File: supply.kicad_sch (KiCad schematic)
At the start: 10 parts, among them U2 AP62301WU-7

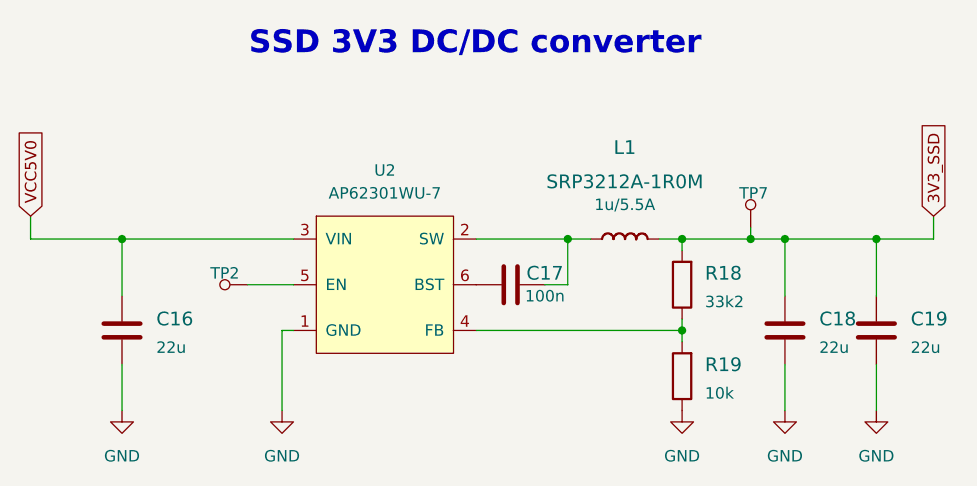
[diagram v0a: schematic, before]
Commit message: Update AP62301WU-7 symbol and footprint
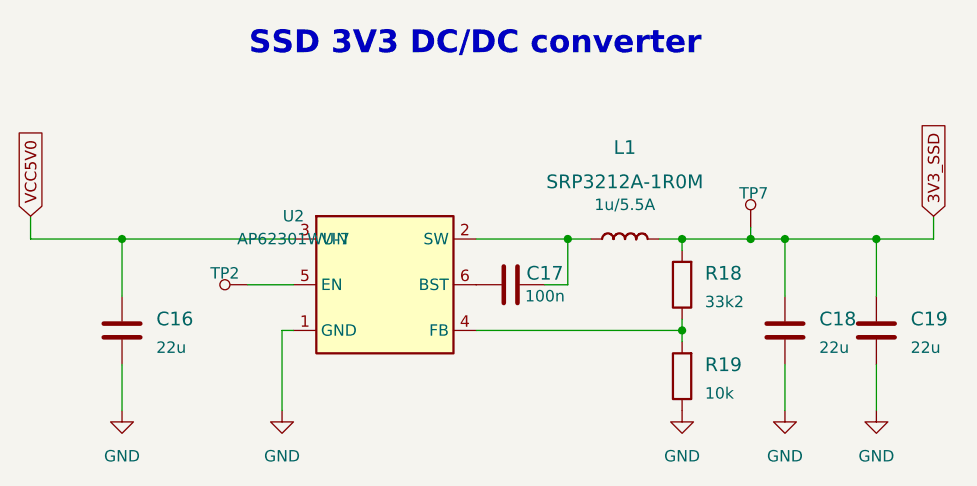
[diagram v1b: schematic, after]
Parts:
- U2: footprint scalenode-cm4-baseboard-footprints:TSOT23-6 -> antmicro-footprints:AP62301WU-7-TSOT23-6; symbol scalenode-cm4-baseboard:AP62301WU-7 -> antmicroDCDCConverters:AP62301WU-7; Author (none) -> Antmicro; Copyright (none) -> Copyright (c) 2023 Antmicro; License (none) -> Apache-2.0
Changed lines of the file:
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@@
     (pin "1")
   )
-  (symbol (lib_id "scalenode-cm4-baseboard:AP62301WU-7") (at 195.58 147.32 0) (unit 1)
+  (symbol (lib_id "antmicroDCDCConverters:AP62301WU-7") (at 185.42 152.4 0) (unit 1)
     (in_bom yes) (on_board yes) (fields_autoplaced)
-    (property "Reference" "U2" (id 0) (at 195.58 134.62 0))
-    (property "Value" "AP62301WU-7" (id 1) (at 195.58 137.16 0))
-    (property "Footprint" "scalenode-cm4-baseboard-footprints:TSOT23-6" (id 2) (at 194.31 163.83 0)
+    (property "Reference" "U2" (id 0) (at 185.42 139.7 0))
+    (property "Value" "AP62301WU-7" (id 1) (at 185.42 142.24 0))
+    (property "Footprint" "antmicro-footprints:AP62301WU-7-TSOT23-6" (id 2) (at 220.98 149.86 0)
+      (effects (font (size 1.27 1.27) (thickness 0.15)) (justify left bottom) hide)
+    )
+    (property "Datasheet" "https://www.diodes.com/assets/Datasheets/AP62300_AP62301_AP62300T.pdf" (id 3) (at 220.98 152.4 0)
+      (effects (font (size 1.27 1.27) (thickness 0.15)) (justify left bottom) hide)
+    )
+    (property "MPN" "AP62301WU-7" (id 4) (at 220.98 154.94 0)
+      (effects (font (size 1.27 1.27) (thickness 0.15)) (justify left bottom) hide)
+    )
+    (property "Manufacturer" "Diodes Incorporated" (id 5) (at 220.98 157.48 0)
+      (effects (font (size 1.27 1.27) (thickness 0.15)) (justify left bottom) hide)
+    )
+    (property "Author" "Antmicro" (id 6) (at 220.98 160.02 0)
+      (effects (font (size 1.27 1.27) (thickness 0.15)) (justify left bottom) hide)
+    )
+    (property "License" "Apache-2.0" (id 7) (at 220.98 162.56 0)
+      (effects (font (size 1.27 1.27) (thickness 0.15)) (justify left bottom) hide)
+    )
+    (property "Copyright" "Copyright (c) 2023 Antmicro" (id 8) (at 185.42 152.4 0)
       (effects (font (size 1.27 1.27)) hide)
     )
-    (property "Datasheet" "https://www.diodes.com/assets/Datasheets/AP62300_AP62301_AP62300T.pdf" (id 3) (at 194.31 156.21 0)
-      (effects (font (size 1.27 1.27)) hide)
-    )
-    (property "MPN" "AP62301WU-7" (id 4) (at 194.31 161.29 0)
-      (effects (font (size 1.27 1.27)) hide)
-    )
-    (property "Manufacturer" "Diodes Incorporated" (id 5) (at 194.31 158.75 0)
-      (effects (font (size 1.27 1.27)) hide)
-    )

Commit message: Delete copyright field
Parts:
- U2: Copyright Copyright (c) 2023 Antmicro -> (none)
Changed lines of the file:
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@@
   )
   (symbol (lib_id "antmicroDCDCConverters:AP62301WU-7") (at 185.42 152.4 0) (unit 1)
-    (in_bom yes) (on_board yes) (fields_autoplaced)
-    (property "Reference" "U2" (id 0) (at 185.42 139.7 0))
-    (property "Value" "AP62301WU-7" (id 1) (at 185.42 142.24 0))
+    (in_bom yes) (on_board yes)
+    (property "Reference" "U2" (id 0) (at 195.072 134.366 0))
+    (property "Value" "AP62301WU-7" (id 1) (at 195.326 136.906 0))
     (property "Footprint" "antmicro-footprints:AP62301WU-7-TSOT23-6" (id 2) (at 220.98 149.86 0)
       (effects (font (size 1.27 1.27) (thickness 0.15)) (justify left bottom) hide)
@@
       (effects (font (size 1.27 1.27) (thickness 0.15)) (justify left bottom) hide)
     )
-    (property "Copyright" "Copyright (c) 2023 Antmicro" (id 8) (at 185.42 152.4 0)
-      (effects (font (size 1.27 1.27)) hide)
-    )
     (pin "1")

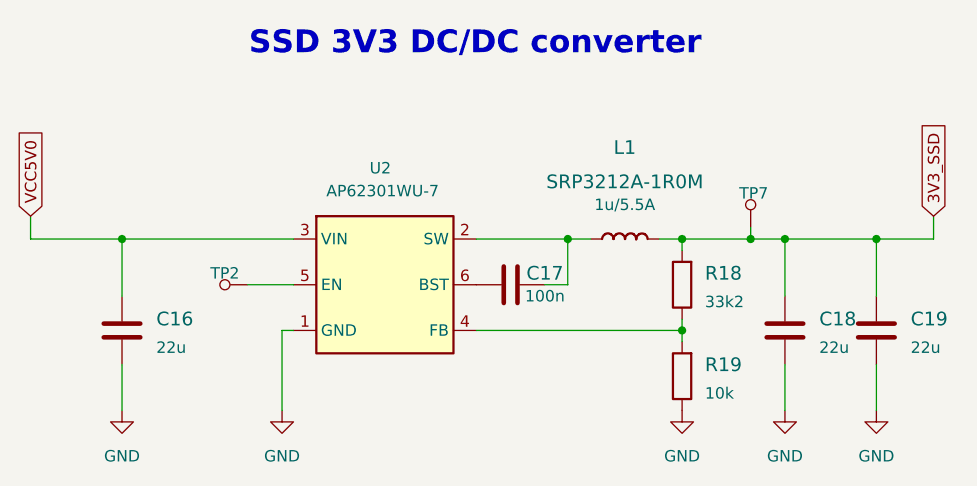
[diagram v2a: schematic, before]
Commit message: Update C1,C2,C3 symbol and footprint
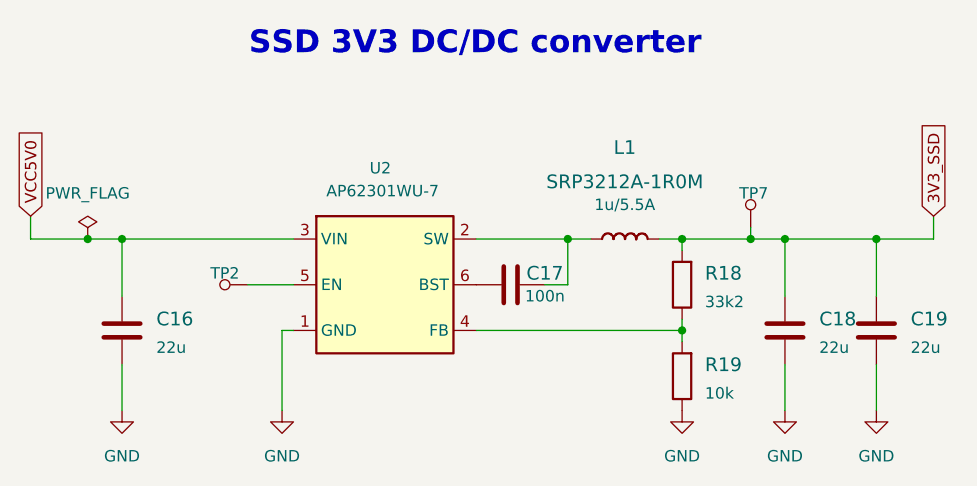
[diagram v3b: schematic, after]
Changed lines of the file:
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@@
   (junction (at 250.19 142.24) (diameter 0) (color 0 0 0 0)
   )
+  (junction (at 162.56 142.24) (diameter 0) (color 0 0 0 0)
+  )
   (junction (at 228.6 152.4) (diameter 0) (color 0 0 0 0)
   )
@@
     (stroke (width 0) (type default) (color 0 0 0 0))
   )
+  (wire (pts (xy 162.56 142.24) (xy 166.37 142.24))
+    (stroke (width 0) (type default) (color 0 0 0 0))
+  )
   (wire (pts (xy 156.21 139.7) (xy 156.21 142.24))
     (stroke (width 0) (type default) (color 0 0 0 0))
@@
     (stroke (width 0) (type default) (color 0 0 0 0))
   )
-  (wire (pts (xy 156.21 142.24) (xy 166.37 142.24))
+  (wire (pts (xy 156.21 142.24) (xy 162.56 142.24))
     (stroke (width 0) (type default) (color 0 0 0 0))
   )
@@
     )
     (pin "1")
+  )
+  (symbol (lib_id "antmicropower:PWR_FLAG") (at 162.56 142.24 0) (unit 1)
+    (in_bom yes) (on_board yes) (fields_autoplaced)
+    (property "Reference" "#FLG0101" (id 0) (at 162.56 140.335 0)
+      (effects (font (size 1.27 1.27)) hide)
+    )
+    (property "Value" "PWR_FLAG" (id 1) (at 162.56 137.16 0))
+    (property "Footprint" "" (id 2) (at 162.56 142.24 0)
+      (effects (font (size 1.27 1.27)) hide)
+    )
+    (property "Datasheet" "" (id 3) (at 162.56 142.24 0)
+      (effects (font (size 1.27 1.27)) hide)
+    )
+    (pin "1")

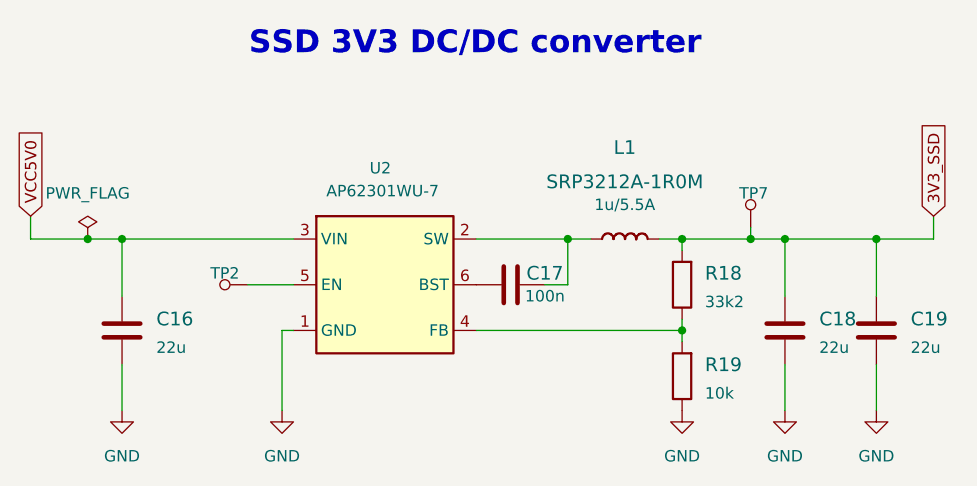
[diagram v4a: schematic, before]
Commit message: Update C13, C17, C21, C37, C51, C54, C55, C56 symbol and footprint
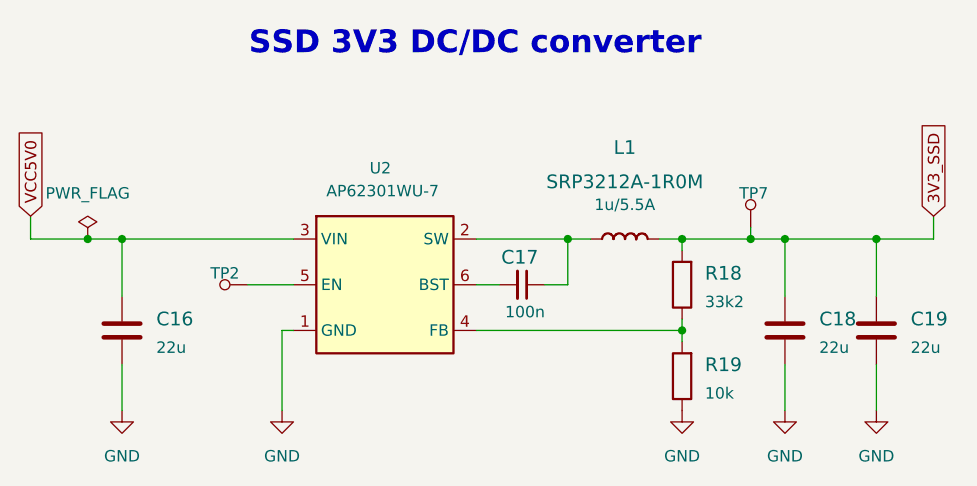
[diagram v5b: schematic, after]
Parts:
- C17: footprint scalenode-cm4-baseboard-footprints:0402-cap -> antmicro-footprints:C_0402_1005Metric; symbol scalenode-cm4-baseboard:C_100n_0402 -> antmicroCapacitors0402:C_100n_0402; Author (none) -> Antmicro; Dielectric (none) -> X5R; License (none) -> Apache-2.0; Voltage (none) -> 50V
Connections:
- net at L1.1 (P), U2.2 (SW): now also C17.1; no longer C17.2
- net at U2.6 (BST): now also C17.2; no longer C17.1
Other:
- moved on the sheet: C17
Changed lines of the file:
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@@
+    (stroke (width 0) (type default) (color 0 0 0 0))
+  )
+  (wire (pts (xy 205.74 147.32) (xy 208.28 147.32))
     (stroke (width 0) (type default) (color 0 0 0 0))
   )
@@
     (pin "1")
   )
-  (symbol (lib_id "scalenode-cm4-baseboard:C_100n_0402") (at 209.55 147.32 90) (unit 1)
+  (symbol (lib_id "antmicroCapacitors0402:C_100n_0402") (at 213.36 147.32 180) (unit 1)
     (in_bom yes) (on_board yes)
-    (property "Reference" "C17" (id 0) (at 213.36 146.05 90)
+    (property "Reference" "C17" (id 0) (at 210.566 144.272 0)
       (effects (font (size 1.524 1.524)))
     )
-    (property "Value" "C_100n_0402" (id 1) (at 213.36 147.32 0)
+    (property "Value" "C_100n_0402" (id 1) (at 213.36 143.51 0)
       (effects (font (size 1.524 1.524)) hide)
     )
-    (property "Footprint" "scalenode-cm4-baseboard-footprints:0402-cap" (id 2) (at 204.47 142.24 0)
-      (effects (font (size 1.524 1.524)) (justify left) hide)
-    )
-    (property "Datasheet" "" (id 3) (at 209.55 147.32 0)
-      (effects (font (size 1.27 1.27)) hide)
-    )
-    (property "Manufacturer" "Murata" (id 4) (at 199.39 142.24 0)
-      (effects (font (size 1.524 1.524)) (justify left) hide)
-    )
-    (property "MPN" "GRM155R61H104KE14D" (id 5) (at 201.93 142.24 0)
-      (effects (font (size 1.524 1.524)) (justify left) hide)
-    )
-    (property "Val" "100n" (id 6) (at 213.36 148.59 90))
+    (property "Footprint" "antmicro-footprints:C_0402_1005Metric" (id 2) (at 193.04 134.62 0)
+      (effects (font (size 1.27 1.27) (thickness 0.15)) (justify left bottom) hide)
+    )
+    (property "Datasheet" "https://search.murata.co.jp/Ceramy/image/img/A01X/G101/ENG/GRM155R61H104KE14-01.pdf" (id 3) (at 193.04 132.08 0)
+      (effects (font (size 1.27 1.27) (thickness 0.15)) (justify left bottom) hide)
+    )
+    (property "Manufacturer" "Murata" (id 4) (at 193.04 127 0)
+      (effects (font (size 1.27 1.27) (thickness 0.15)) (justify left bottom) hide)
+    )
+    (property "MPN" "GRM155R61H104KE14D" (id 5) (at 193.04 129.54 0)
+      (effects (font (size 1.27 1.27) (thickness 0.15)) (justify left bottom) hide)
+    )
+    (property "Val" "100n" (id 6) (at 213.36 149.606 0)
+      (effects (font (size 1.27 1.27) (thickness 0.15)) (justify left bottom))
+    )
+    (property "License" "Apache-2.0" (id 7) (at 193.04 124.46 0)
+      (effects (font (size 1.27 1.27) (thickness 0.15)) (justify left bottom) hide)
+    )
+    (property "Author" "Antmicro" (id 8) (at 193.04 121.92 0)
+      (effects (font (size 1.27 1.27) (thickness 0.15)) (justify left bottom) hide)
+    )
+    (property "Voltage" "50V" (id 9) (at 193.04 119.38 0)
+      (effects (font (size 1.27 1.27)) (justify left bottom) hide)
+    )
+    (property "Dielectric" "X5R" (id 10) (at 193.04 116.84 0)
+      (effects (font (size 1.27 1.27)) (justify left bottom) hide)
+    )
     (pin "1")
     (pin "2")

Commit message: Update C16, C18, C19 symbol and footprint
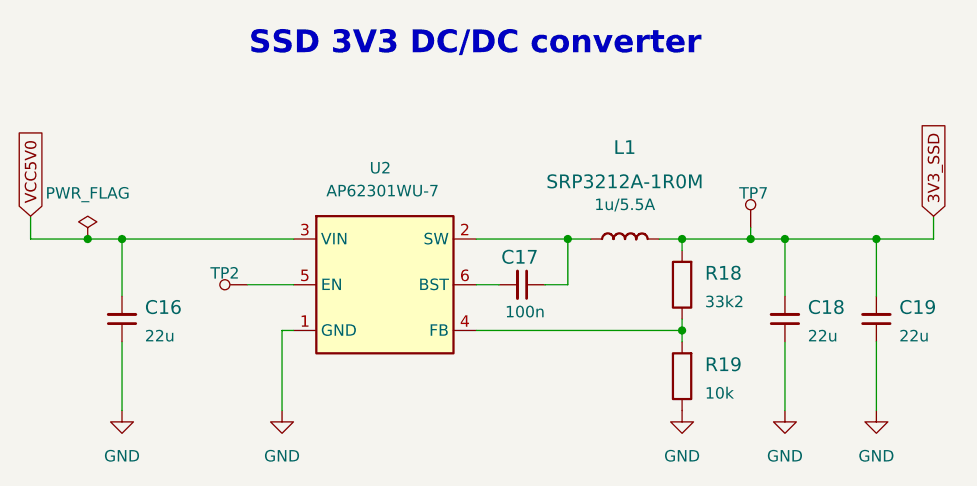
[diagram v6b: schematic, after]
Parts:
- C16, C18, C19: footprint scalenode-cm4-baseboard-footprints:0805-cap -> antmicro-footprints:C_0805_2012Metric; symbol scalenode-cm4-baseboard:C_22u_0805_10V -> antmicroCapacitorsmisc:C_22u_0805_10V; Author (none) -> Antmicro; License (none) -> Apache-2.0
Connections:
- net 3V3_SSD: now also C18.2, C19.2; no longer C18.1, C19.1
- net GND: now also C16.1, C18.1, C19.1; no longer C16.2, C18.2, C19.2
- net VCC5V0: now also C16.2; no longer C16.1
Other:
- moved on the sheet: C16, C18, C19

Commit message: Update L1 symbol and footprint
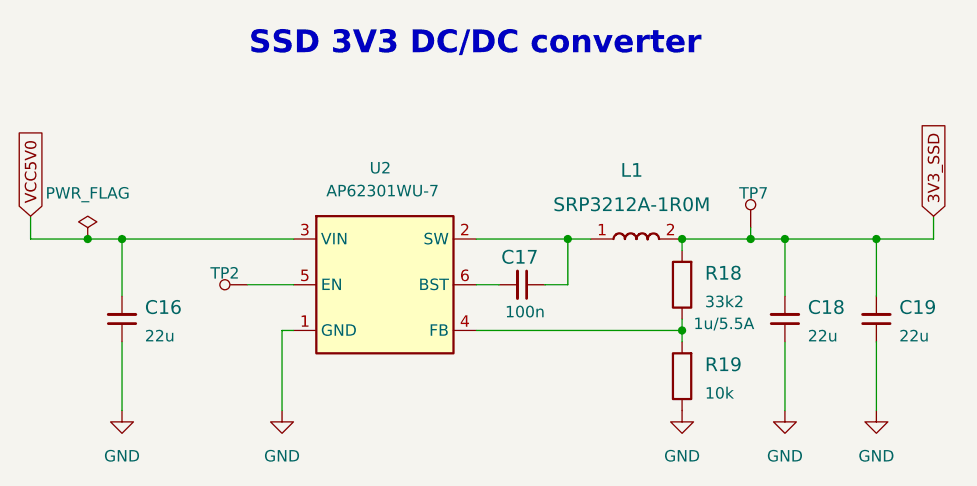
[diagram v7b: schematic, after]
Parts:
- L1: footprint scalenode-cm4-baseboard-footprints:SRP3212 -> antmicro-footprints:SRP3212; symbol scalenode-cm4-baseboard:SRP3212A-1R0M -> antmicroFixedInductors:SRP3212A-1R0M; Author (none) -> Antmicro; License (none) -> Apache-2.0; Manufacturer BOURNS -> Bourns
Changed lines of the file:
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@@
-    (stroke (width 0) (type default) (color 0 0 0 0))
-  )
-  (wire (pts (xy 226.06 142.24) (xy 228.6 142.24))
     (stroke (width 0) (type default) (color 0 0 0 0))
   )
@@
     (pin "1")
   )
-  (symbol (lib_id "scalenode-cm4-baseboard:SRP3212A-1R0M") (at 222.25 142.24 0) (unit 1)
-    (in_bom yes) (on_board yes) (fields_autoplaced)
-    (property "Reference" "L1" (id 0) (at 222.2373 132.08 0)
+  (symbol (lib_id "antmicroFixedInductors:SRP3212A-1R0M") (at 218.44 142.24 0) (unit 1)
+    (in_bom yes) (on_board yes)
+    (property "Reference" "L1" (id 0) (at 223.012 134.62 0)
       (effects (font (size 1.524 1.524)))
     )
-    (property "Value" "SRP3212A-1R0M" (id 1) (at 222.2373 135.89 0)
+    (property "Value" "SRP3212A-1R0M" (id 1) (at 223.012 138.43 0)
       (effects (font (size 1.524 1.524)))
     )
-    (property "Footprint" "scalenode-cm4-baseboard-footprints:SRP3212" (id 2) (at 222.25 154.94 0)
-      (effects (font (size 1.524 1.524)) hide)
-    )
-    (property "Datasheet" "https://www.mouser.pl/datasheet/2/54/srp3212-2948733.pdf" (id 3) (at 222.25 154.94 0)
-      (effects (font (size 1.524 1.524)) hide)
-    )
-    (property "Manufacturer" "BOURNS" (id 4) (at 220.345 153.035 0)
-      (effects (font (size 1.27 1.27)) hide)
-    )
-    (property "MPN" "SRP3212A-1R0M" (id 5) (at 224.155 154.94 0)
-      (effects (font (size 1.27 1.27)) hide)
-    )
-    (property "MaxCur" "5.5A" (id 6) (at 219.075 158.75 0)
-      (effects (font (size 1.27 1.27)) hide)
-    )
-    (property "Size" "3.2x2.5" (id 7) (at 220.98 156.845 0)
-      (effects (font (size 1.27 1.27)) hide)
-    )
-    (property "Val" "1u/5.5A" (id 8) (at 222.2373 138.43 0))
+    (property "Footprint" "antmicro-footprints:SRP3212" (id 2) (at 229.87 154.94 0)
+      (effects (font (size 1.27 1.27) (thickness 0.15)) (justify left bottom) hide)
+    )
+    (property "Datasheet" "https://www.mouser.pl/datasheet/2/54/srp3212-2948733.pdf" (id 3) (at 229.87 157.48 0)
+      (effects (font (size 1.27 1.27) (thickness 0.15)) (justify left bottom) hide)
+    )
+    (property "Manufacturer" "Bourns" (id 4) (at 229.87 160.02 0)
+      (effects (font (size 1.27 1.27) (thickness 0.15)) (justify left bottom) hide)
+    )
+    (property "MPN" "SRP3212A-1R0M" (id 5) (at 229.87 162.56 0)
+      (effects (font (size 1.27 1.27) (thickness 0.15)) (justify left bottom) hide)
+    )
+    (property "MaxCur" "5.5A" (id 6) (at 229.87 165.1 0)
+      (effects (font (size 1.27 1.27) (thickness 0.15)) (justify left bottom) hide)
+    )
+    (property "Size" "3.2x2.5" (id 7) (at 229.87 167.64 0)
+      (effects (font (size 1.27 1.27) (thickness 0.15)) (justify left bottom) hide)
+    )
+    (property "Val" "1u/5.5A" (id 8) (at 229.87 152.4 0)
+      (effects (font (size 1.27 1.27) (thickness 0.15)) (justify left bottom))
+    )
+    (property "Author" "Antmicro" (id 9) (at 229.87 170.18 0)
+      (effects (font (size 1.27 1.27) (thickness 0.15)) (justify left bottom) hide)
+    )
+    (property "License" "Apache-2.0" (id 10) (at 229.87 172.72 0)
+      (effects (font (size 1.27 1.27) (thickness 0.15)) (justify left bottom) hide)
+    )
     (pin "1")
     (pin "2")
